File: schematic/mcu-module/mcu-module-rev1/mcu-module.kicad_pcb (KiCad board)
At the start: 2 copper layers, 44.9 x 26 mm, 22 parts, among them P1 MCU1, P2 MICROSD-SDIO-CD, P3 SWD, P4 MCU2, U1 STM32F103RE, X1 32768Hz, X2 8MHz

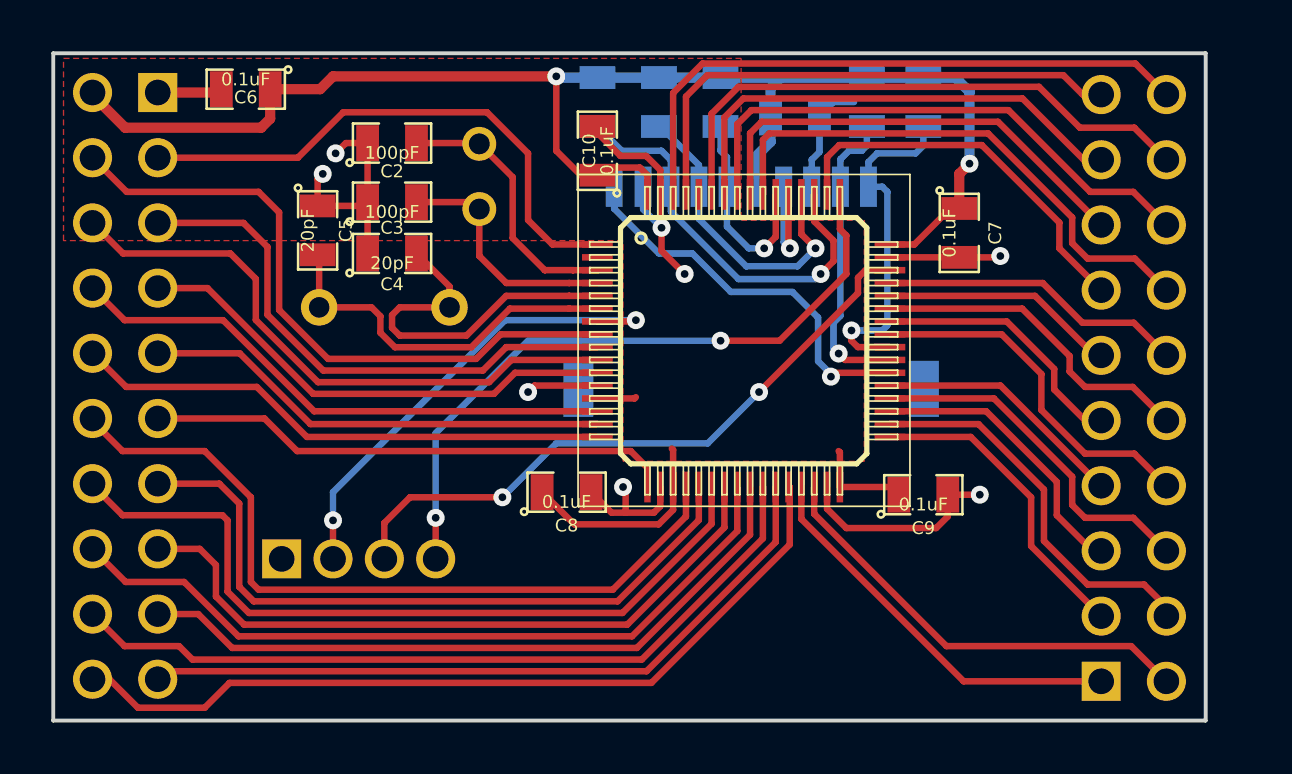
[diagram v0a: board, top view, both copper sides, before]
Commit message: RTC and ADC support beginning. RTC wotks from external quartz
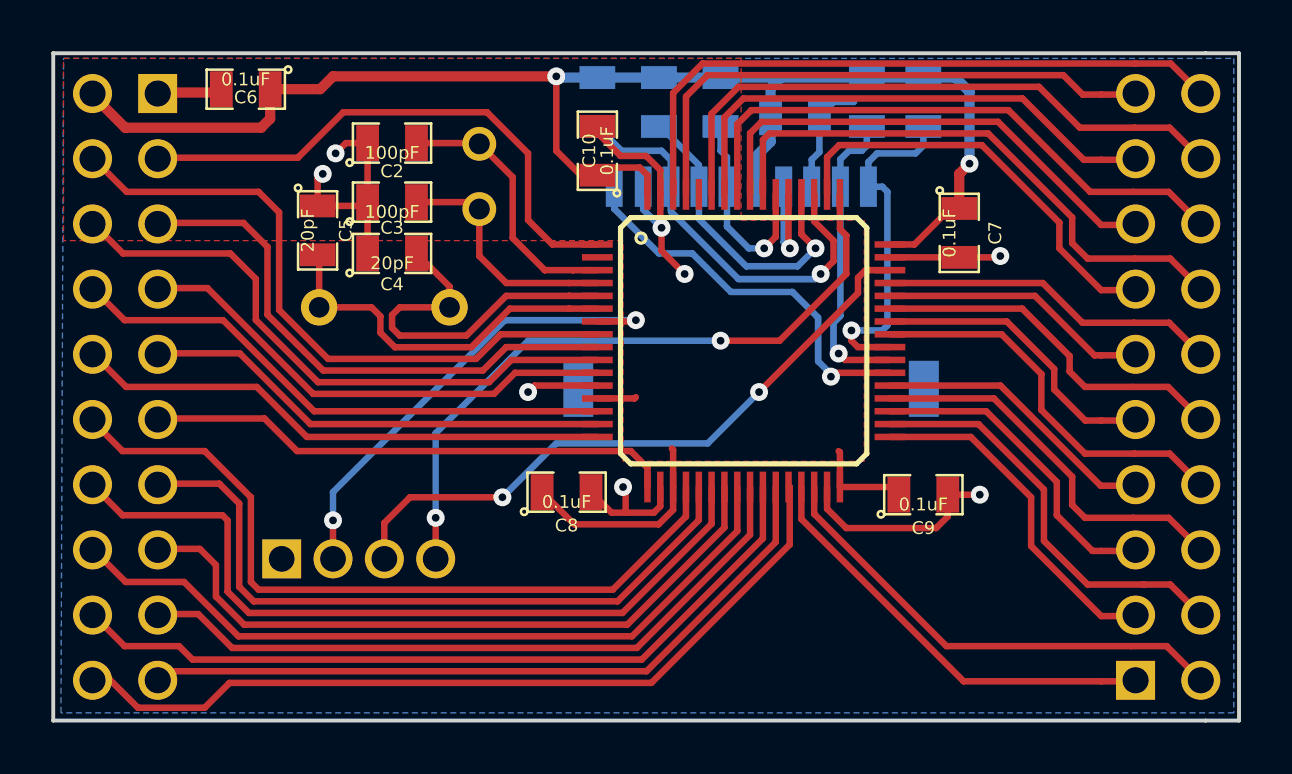
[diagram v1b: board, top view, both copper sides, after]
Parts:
- moved P4 1.34 mm to (106.1, 59.1)
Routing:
- net N-0000041: track 12.2 -> 13.6 mm
- net N-0000038: track 9.85 -> 11.2 mm
- net N-0000032: track 17.9 -> 19.3 mm
- net N-0000036: track 10.3 -> 11.7 mm
- net N-0000033: track 15.3 -> 16.6 mm
- net N-0000030: track 19.0 -> 20.3 mm
- net N-0000028: track 20.6 -> 22.0 mm
- net N-0000035: track 9.19 -> 10.5 mm
- net N-0000039: track 11.2 -> 12.6 mm
- net N-0000044: track 15.5 -> 16.9 mm
- net N-0000042: track 17.5 -> 18.8 mm
- net N-0000027: track 13.9 -> 15.2 mm
- net N-0000034: track 11.9 -> 13.3 mm
- net N-0000045: track 21.1 -> 22.4 mm
- net N-0000031: track 21.5 -> 22.9 mm
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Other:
- board size 44.9 x 26 mm -> 46.2 x 26 mm

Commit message: MCU module rev2 done
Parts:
- removed P2: MICROSD-SDIO-CD, MICROSD-CD
- added ?: , MICROSD-CD-112IJ, B.Cu at (89.0, 51.3)
- added FB1: , SM0805, F.Cu at (70.0, 49.1)
- ?: renamed from U1; value STM32F103RE -> (none)
- C2, C3: value 100pF -> 20pF
- X1: footprint crystal-TC26H -> TC26H-fixed
- moved C6 0.28 mm to (70.0, 47.3)
- moved X1 0.14 mm to (79.2, 50.8)
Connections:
- P1 pad 2: +3.3V -> N-0000023
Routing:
- net +3.3V: track 72.4 -> 65.5 mm
- net N-0000023: track 0.00 -> 5.44 mm
- net N-0000052: track 13.6 -> 12.0 mm
- net N-0000025: track 25.5 -> 27.0 mm
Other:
- board text added: "Caustic LT system MCU board rev3"
- board text added: "microSD 112I/J- TDAR-R"
- board text added: "stm32 f103ret6"
- board text removed: "Caustic LT system MCU board rev1.0"
- board text removed: "SWD"

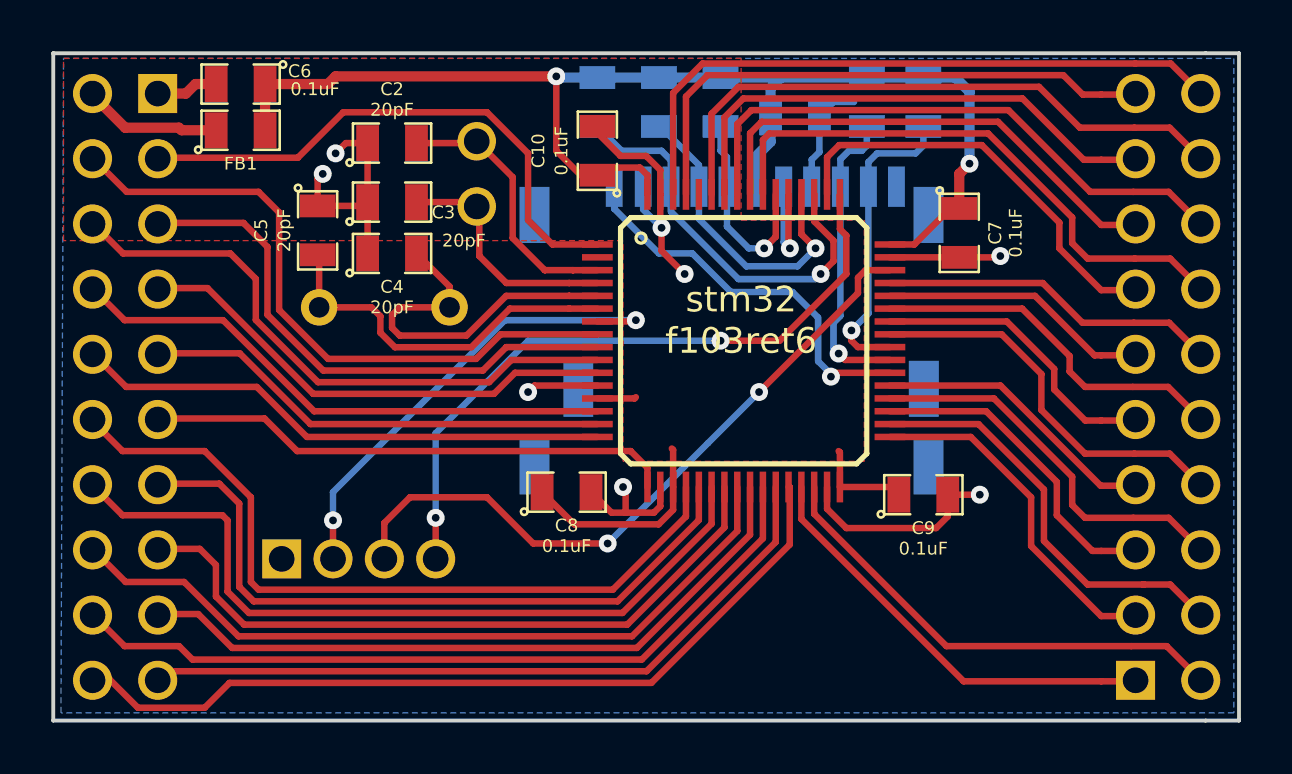
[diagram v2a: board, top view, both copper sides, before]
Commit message: Ferrite bead added to MCU module
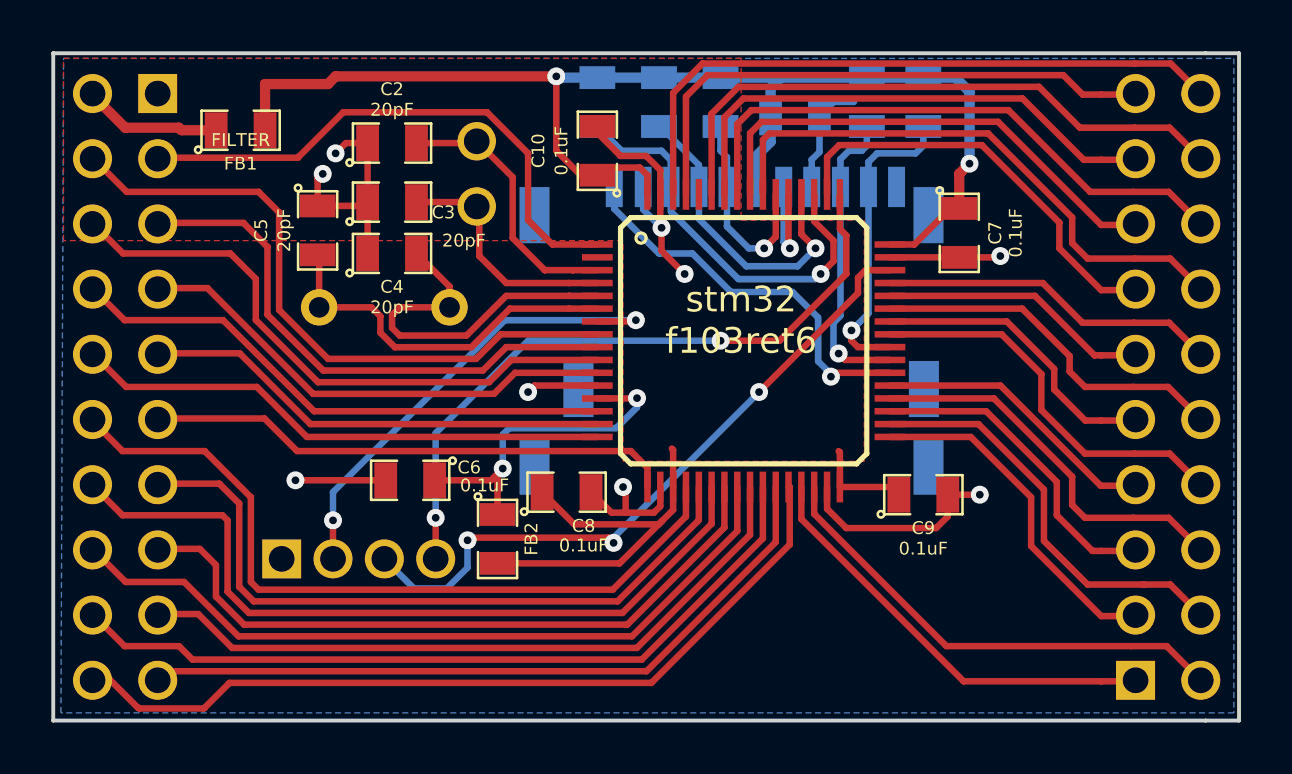
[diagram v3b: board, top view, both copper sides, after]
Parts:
- removed ?: , LQFP64-0.254mm-pins
- removed ?: , MICROSD-CD-112IJ
- added FB2: FILTER, SM0805, F.Cu at (80.0, 65.0)
- added P2: MICROSD-SDIO-CD, MICROSD-CD-112IJ, B.Cu at (89.0, 51.3)
- added U1: STM32F103RE, LQFP64-0.254mm-pins, F.Cu at (89.6, 57.3)
- FB1: value (none) -> FILTER
- moved C6 16.8 mm to (76.6, 62.7)
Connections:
- C6 pad 1: +3.3V -> N-0000048
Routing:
- net N-0000023: track 0.00 -> 15.4 mm, vias 0 -> 1
- net N-0000017 (its old number): track 15.4 -> 0.00 mm, vias 1 -> 0
- net N-0000048: track 0.00 -> 13.6 mm, vias 0 -> 2
- net +3.3V: track 65.5 -> 71.1 mm
- net N-0000054 (its old number): track 4.62 -> 0.00 mm, vias 1 -> 0
- net N-0000053: track 0.00 -> 4.62 mm, vias 0 -> 1
- net GND: track 45.8 -> 46.9 mm, vias 8 -> 9
- net N-0000039: track 27.0 -> 26.6 mm, vias 2 -> 3
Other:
- board text added: "Caustic LT system MCU board rev3.1"
- board text removed: "Caustic LT system MCU board rev3"

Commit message: New sensor module for LW round plastic sensor; leds are 1206, capacitors fixed
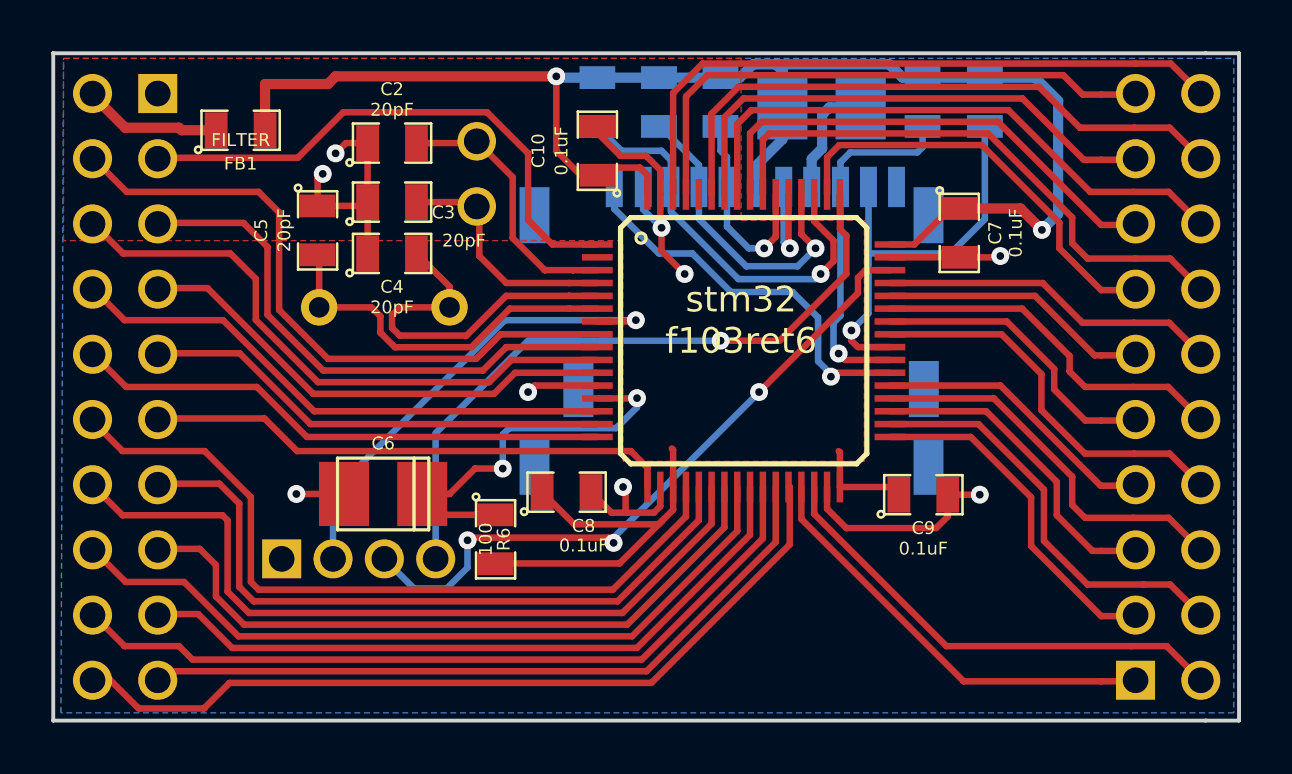
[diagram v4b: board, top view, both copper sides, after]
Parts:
- removed FB2: FILTER, SM0805
- added R6: 100, SM0805, F.Cu at (79.9, 65.0)
- C1, C6: value 0.1uF -> 100uF; footprint SM0805 -> c_tant_B
- moved R3 2.40 mm to (99.0, 48.0)
- moved R4 2.17 mm to (96.6, 48.0)
- moved C6 1.18 mm to (75.6, 63.3), turned to 0 degrees
- moved C1 1.11 mm to (92.6, 48.2)
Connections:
- C1 pad 1: GND -> +3.3V
- C1 pad 2: +3.3V -> GND
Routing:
- net +3.3V: track 71.1 -> 78.1 mm
- net N-0000056: track 12.0 -> 16.6 mm
- net N-0000055: track 11.9 -> 14.0 mm
- net N-0000048: track 13.6 -> 15.7 mm
- net GND: track 46.9 -> 45.4 mm
- net N-0000044: vias 2 -> 1
- net N-0000039: vias 2 -> 1
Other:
- net class Default: trace_width 0.254 -> 0.4
